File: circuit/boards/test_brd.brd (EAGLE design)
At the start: 160 x 100 mm, 12 parts, among them Q1 2N5484, X1 JST-XH-02-PIN-LONG-PAD, X2 JST-XH-02-PIN-LONG-PAD, X3 JST-XH-05-PIN-LONG-PAD

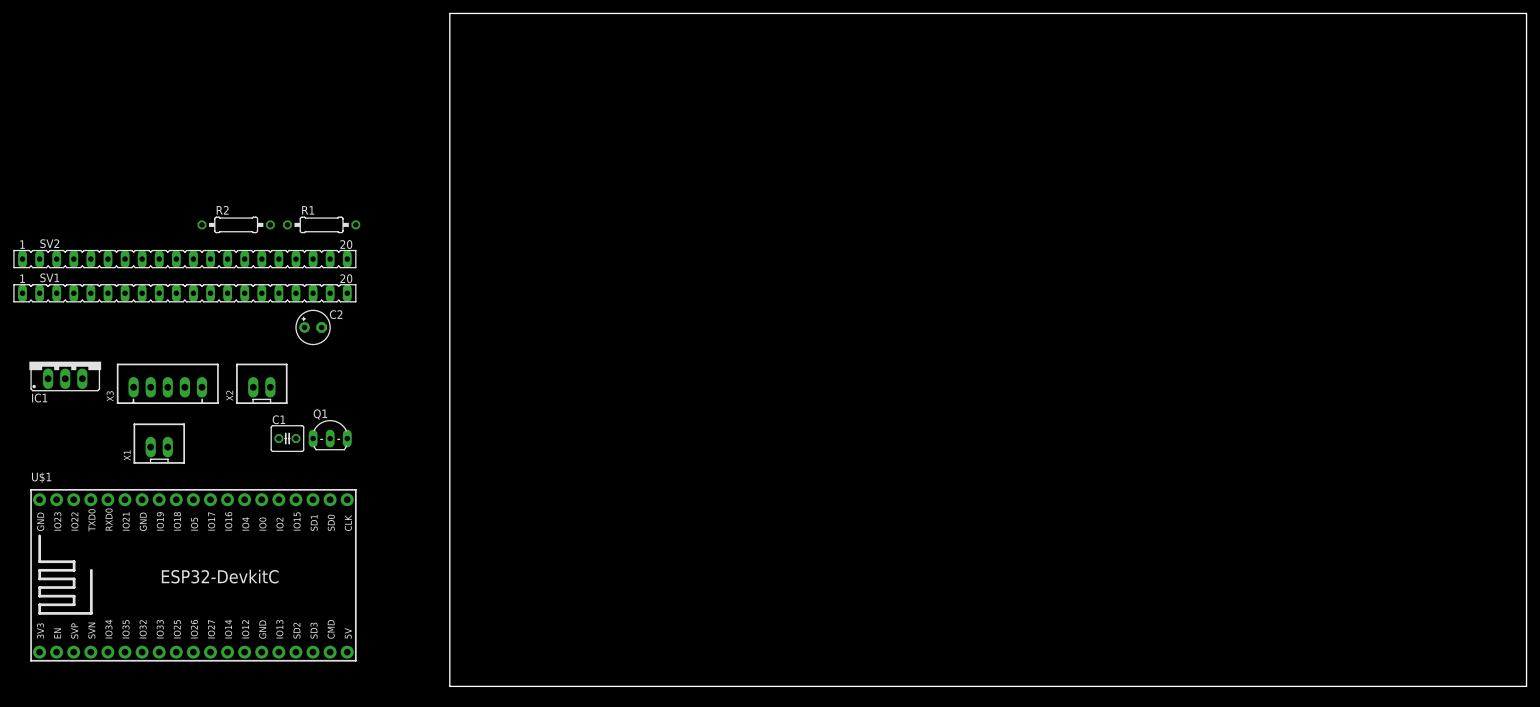
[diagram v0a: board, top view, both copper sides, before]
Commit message: gridを表示
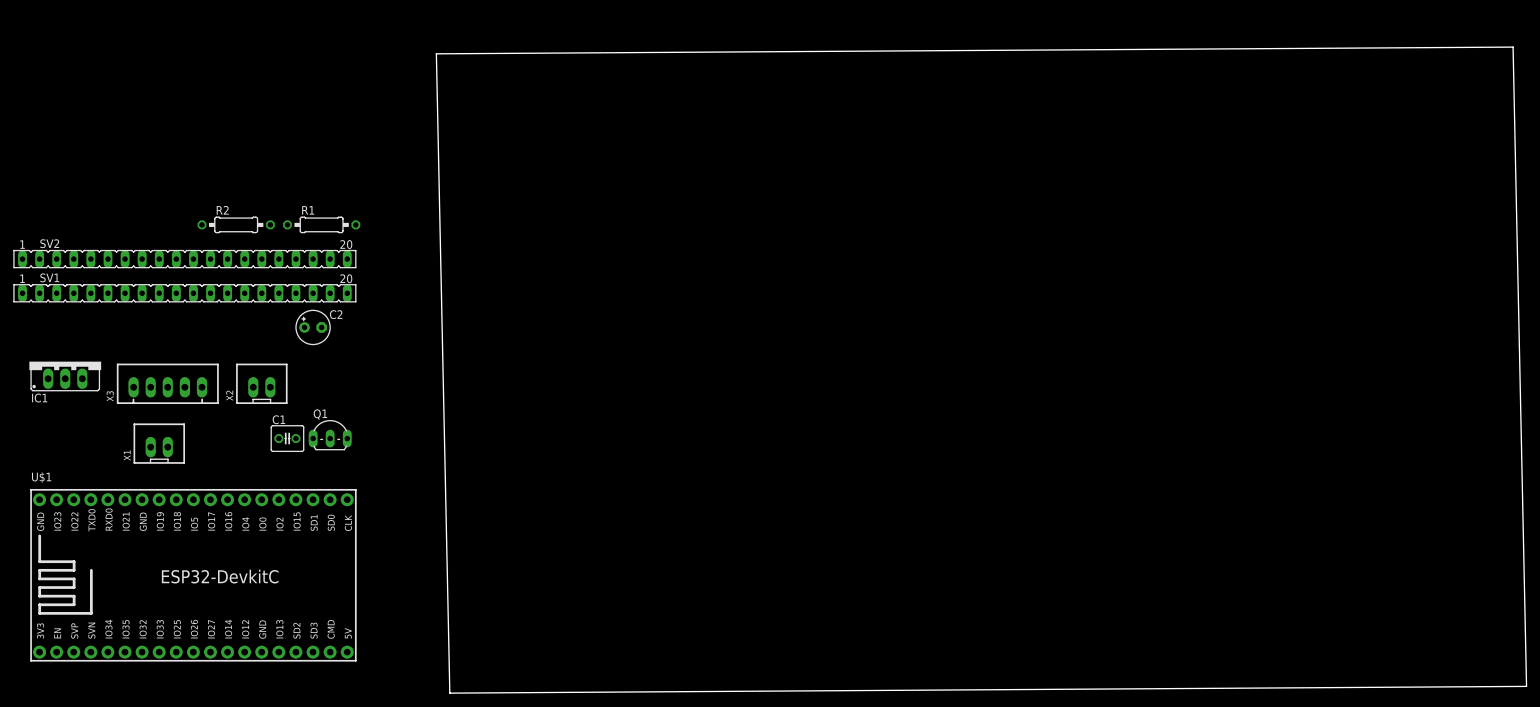
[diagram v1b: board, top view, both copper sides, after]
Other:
- board size 160 x 100 mm -> 162 x 96 mm
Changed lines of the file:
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@@
 <setting verticaltext="up"/>
 </settings>
-<grid distance="50" unitdist="mil" unit="mil" style="lines" multiple="1" display="no" altdistance="5" altunitdist="mil" altunit="mil"/>
+<grid distance="1" unitdist="mm" unit="mm" style="lines" multiple="1" display="yes" altdistance="0.1" altunitdist="mm" altunit="mm"/>
 <layers>
 <layer number="1" name="Top" color="4" fill="1" visible="yes" active="yes"/>
@@
 <board>
 <plain>
-<wire x1="0" y1="0" x2="160" y2="0" width="0" layer="20"/>
-<wire x1="160" y1="0" x2="160" y2="100" width="0" layer="20"/>
-<wire x1="160" y1="100" x2="0" y2="100" width="0" layer="20"/>
-<wire x1="0" y1="100" x2="0" y2="0" width="0" layer="20"/>
+<wire x1="0" y1="-1" x2="160" y2="0" width="0" layer="20"/>
+<wire x1="160" y1="0" x2="158" y2="95" width="0" layer="20"/>
+<wire x1="158" y1="95" x2="-2" y2="94" width="0" layer="20"/>
+<wire x1="-2" y1="94" x2="0" y2="-1" width="0" layer="20"/>
 </plain>
 <attributes>

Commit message: ベタを作成
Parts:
- moved R1 125.1 mm to (106.0, 74.6)
- moved Q1 112.1 mm to (94.2, 40.8)
- moved C2 107.0 mm to (86.7, 53.3)
- moved R2 102.2 mm to (70.2, 75.6)
- moved X2 99.3 mm to (71.1, 52.5)
- moved X1 99.2 mm to (55.8, 29.6)
- moved C1 90.4 mm to (65.9, 45.8)
- moved X3 76.5 mm to (33.1, 29.4)
- moved SV1 70.1 mm to (30.6, 54.4)
- moved IC1 70.0 mm to (12.8, 46.3)
- moved SV2 69.0 mm to (29.6, 65.5)
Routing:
- net N$3: track 0.00 -> 259.2 mm
- net N$2: track 0.00 -> 107.2 mm
- net N$4: track 0.00 -> 77.1 mm
- net N$1: track 0.00 -> 74.3 mm
- net N$9: track 0.00 -> 59.7 mm
- net N$7: track 0.00 -> 45.4 mm
- net N$5: track 0.00 -> 43.5 mm
- net N$6: track 0.00 -> 28.2 mm
- net N$8: track 0.00 -> 27.7 mm
- added copper zone on layer 16, net GROUND
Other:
- board size 162 x 96 mm -> 163 x 95 mm
